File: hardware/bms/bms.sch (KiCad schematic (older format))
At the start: 199 parts, among them J1 Conn_01x08, J10 Conn_01x02, J11 Conn_01x02, J12 Conn_01x02, J13 Conn_01x10, J14 Conn_01x02, J15 Conn_01x02, J16 Cell Bypass, J2 Conn_01x04, J3 USB_B_Micro, J4 Conn_01x05, J5 Conn_01x04, J6 Conn_01x04, J7 Conn_01x03, J8 Conn_01x03, J9 Conn_01x02, M1 MountingHole, M2 MountingHole, M3 MountingHole, M4 MountingHole, M5 MountingHole, M6 MountingHole, Q1 BC817, Q10 ZXMP4A16G, Q11 IRF540N, Q12 IRF540N, Q13 BSS138, Q14 IRF540N, Q15 BSS138, Q16 BSS138, Q2 ZXMP4A16G, Q3 BSS138, Q4 BS170, Q5 IRF9540N, Q6 BC847, Q7 IRF9540N, Q8 BSS138, Q9 ZXMP4A16G, SW1 SW_DIP_x03, U1 USBLC6-2SC6, U2 STM32F042C6Tx, U3 TPS560430x3F, U4 TCAN334, U5 MAX485E, U6 LM5164DDAR, U7 LSI94202, Y1 8MHz

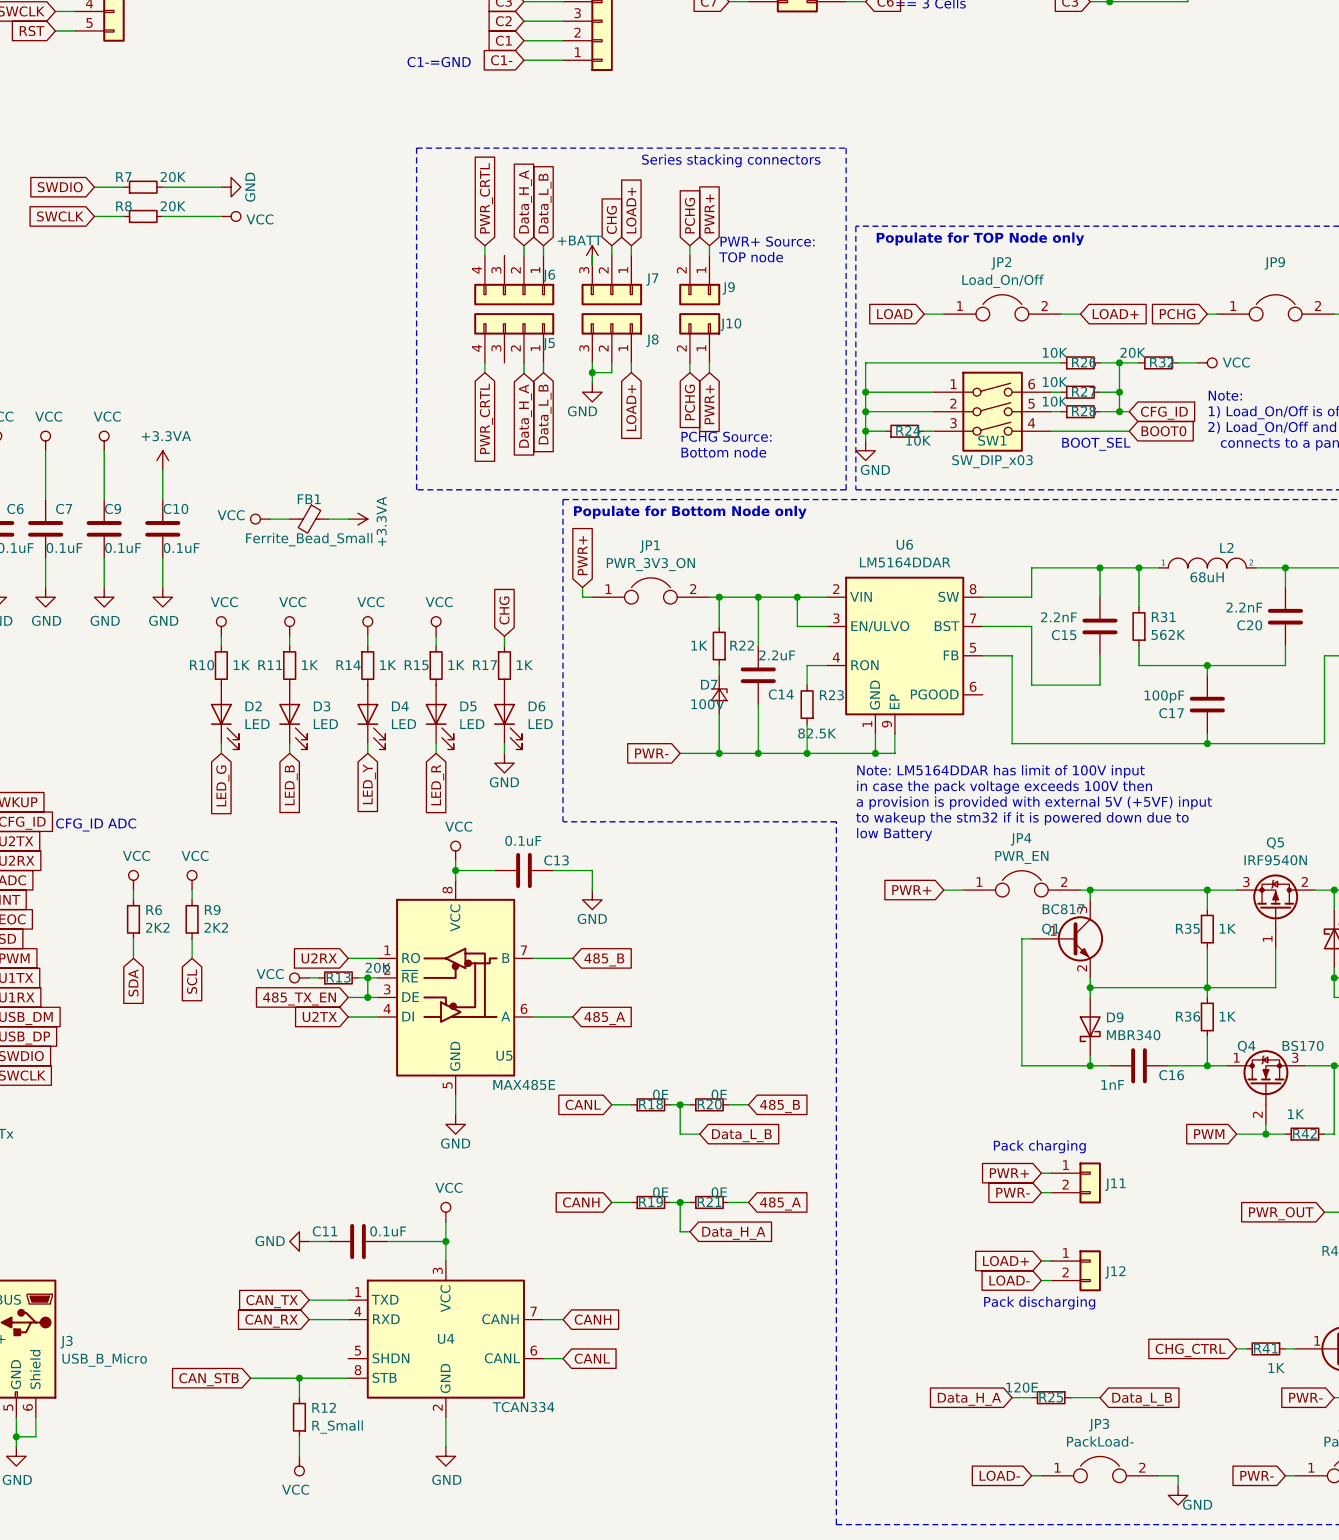
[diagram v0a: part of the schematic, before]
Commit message: Changed connection to support series and parallel stacking
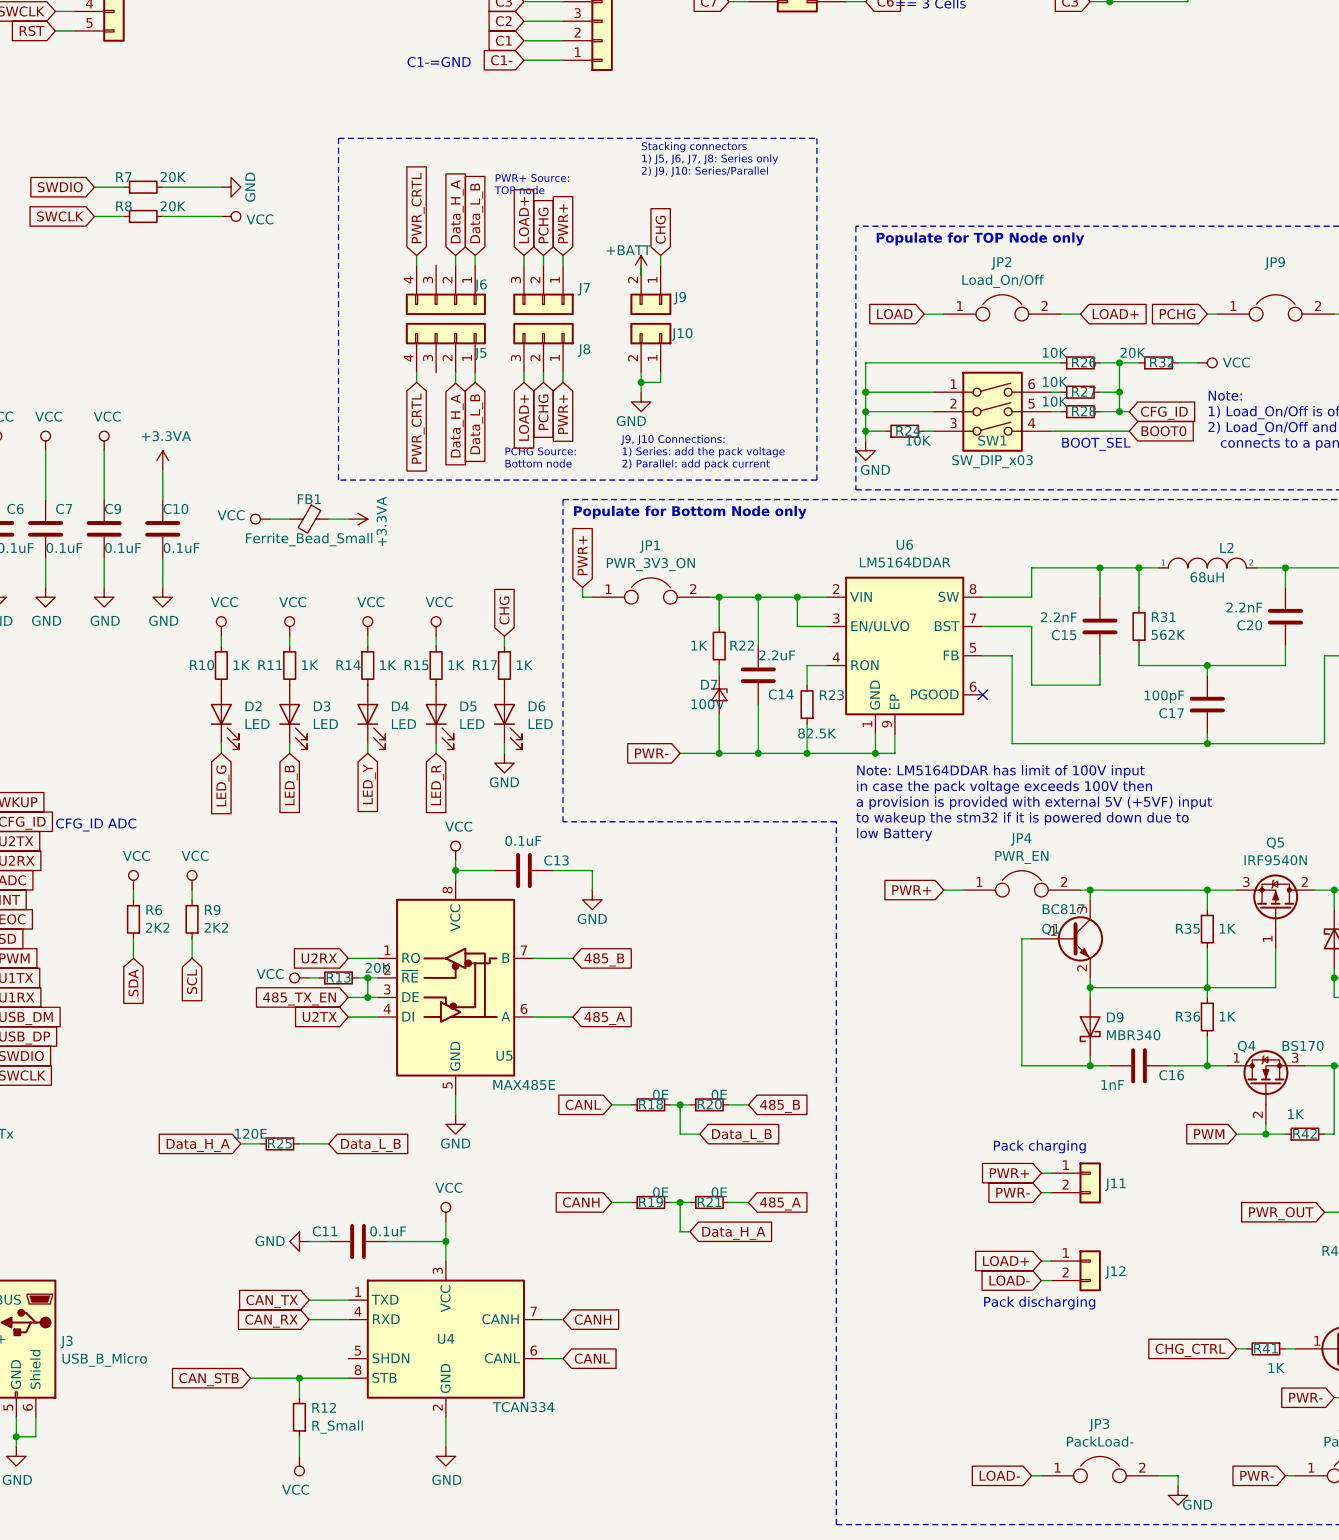
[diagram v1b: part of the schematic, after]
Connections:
- net +BATT: now also J9.2 (Pin_2); no longer J7.3 (Pin_3)
- net CHG: now also J9.1 (Pin_1); no longer J7.2 (Pin_2)
- net GND: now also J10.1 (Pin_1), J10.2 (Pin_2); no longer J8.2 (Pin_2), J8.3 (Pin_3)
- net LOAD+: now also J7.3 (Pin_3), J8.3 (Pin_3); no longer J7.1 (Pin_1), J8.1 (Pin_1)
- net PCHG: now also J7.2 (Pin_2), J8.2 (Pin_2); no longer J10.2 (Pin_2), J9.2 (Pin_2)
- net PWR+: now also J7.1 (Pin_1), J8.1 (Pin_1); no longer J10.1 (Pin_1), J9.1 (Pin_1)
- no-connect marks 6 -> 7
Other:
- note added: "J9, J10 Connections:\n1) Series: add the pack voltage\n2) Parallel: add pack current"
- note added: "Stacking connectors\n1) J5, J6, J7, J8: Series only\n2) J9, J10: Series/Parallel"
- note removed: "Series stacking connectors"
- moved on the sheet: J10, J5, J6, J7, J8, J9, R25
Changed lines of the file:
@@
 L Device:R_Small R25
 U 1 1 5E91A3BE
-P 8600 10400
-F 0 "R25" V 8600 10400 50  0000 C CNN
-F 1 "120E" V 8550 10250 50  0000 C CNN
-F 2 "Resistor_SMD:R_0603_1608Metric_Pad1.05x0.95mm_HandSolder" H 8600 10400 50  0001 C CNN
-F 3 "~" H 8600 10400 50  0001 C CNN
-	1    8600 10400
+P 4650 9100
+F 0 "R25" V 4650 9100 50  0000 C CNN
+F 1 "120E" V 4600 8950 50  0000 C CNN
+F 2 "Resistor_SMD:R_0603_1608Metric_Pad1.05x0.95mm_HandSolder" H 4650 9100 50  0001 C CNN
+F 3 "~" H 4650 9100 50  0001 C CNN
+	1    4650 9100
 	0    1    1    0
 $EndComp
-Text GLabel 8400 10400 0    50   Input ~ 0
+Text GLabel 4450 9100 0    50   Input ~ 0
 Data_H_A
-Text GLabel 8850 10400 2    50   Input ~ 0
+Text GLabel 4900 9100 2    50   Input ~ 0
 Data_L_B
 Wire Wire Line
-	8400 10400 8500 10400
+	4450 9100 4550 9100
 Wire Wire Line
-	8700 10400 8850 10400
+	4750 9100 4900 9100
 Text GLabel 5000 8450 0    50   Input ~ 0
 U2TX
@@
 L power:+BATT #PWR0144
 U 1 1 5F326BD9
-P 6250 4600
-F 0 "#PWR0144" H 6250 4450 50  0001 C CNN
-F 1 "+BATT" H 6184 4725 50  0000 C CNN
-F 2 "" H 6250 4600 50  0001 C CNN
-F 3 "" H 6250 4600 50  0001 C CNN
-	1    6250 4600
+P 6500 4650
+F 0 "#PWR0144" H 6500 4500 50  0001 C CNN
+F 1 "+BATT" H 6434 4775 50  0000 C CNN
+F 2 "" H 6500 4650 50  0001 C CNN
+F 3 "" H 6500 4650 50  0001 C CNN
+	1    6500 4650
 	1    0    0    -1
 $EndComp
 Wire Wire Line
-	6350 5100 6350 5150
-Text GLabel 5900 5154 3    50   Input ~ 0
+	6600 5150 6600 5200
+Text GLabel 5550 5204 3    50   Input ~ 0
 Data_H_A
-Text GLabel 6000 5150 3    50   Input ~ 0
+Text GLabel 5650 5200 3    50   Input ~ 0
 Data_L_B
 Connection ~ 12000 7500
@@
 Wire Wire Line
 	1400 8450 1750 8450
-Text GLabel 5700 5150 3    50   Input ~ 0
+Text GLabel 5350 5200 3    50   Input ~ 0
 PWR_CRTL
 Text GLabel 6750 9550 2    50   Input ~ 0
@@
 	9550 10150 9600 10150
 Wire Wire Line
-	6250 4600 6250 4550
+	6500 4650 6500 4600
 Wire Wire Line
-	6350 4500 6350 4550
+	6600 4550 6600 4600
 Wire Wire Line
-	6250 5200 6250 5150
-Text GLabel 6000 4500 1    50   Input ~ 0
+	6500 5250 6500 5200
+Text GLabel 5650 4550 1    50   Input ~ 0
 Data_L_B
-Text GLabel 5900 4500 1    50   Input ~ 0
+Text GLabel 5550 4550 1    50   Input ~ 0
 Data_H_A
-Text GLabel 6350 4500 1    50   Input ~ 0
+Text GLabel 6600 4550 1    50   Input ~ 0
 CHG
 $Comp
 L power:GND #PWR0147
 U 1 1 5E739987
-P 6250 5200
-F 0 "#PWR0147" H 6250 4950 50  0001 C CNN
-F 1 "GND" H 6200 5050 50  0000 C CNN
-F 2 "" H 6250 5200 50  0001 C CNN
-F 3 "" H 6250 5200 50  0001 C CNN
-	1    6250 5200
+P 6500 5250
+F 0 "#PWR0147" H 6500 5000 50  0001 C CNN
+F 1 "GND" H 6450 5100 50  0000 C CNN
+F 2 "" H 6500 5250 50  0001 C CNN
+F 3 "" H 6500 5250 50  0001 C CNN
+	1    6500 5250
 	1    0    0    -1
 $EndComp
@@
 L Connector_Generic:Conn_01x04 J5
 U 1 1 5E7A8731
-P 5900 4750
-F 0 "J5" V 6150 4850 50  0000 L CNN
-F 1 "Conn_01x04" H 5980 4651 50  0001 L CNN
-F 2 "Connector_Molex:Molex_KK-254_AE-6410-04A_1x04_P2.54mm_Vertical" H 5900 4750 50  0001 C CNN
-F 3 "~" H 5900 4750 50  0001 C CNN
-	1    5900 4750
+P 5550 4800
+F 0 "J5" V 5800 4900 50  0000 L CNN
+F 1 "Conn_01x04" H 5630 4701 50  0001 L CNN
+F 2 "Connector_Molex:Molex_KK-254_AE-6410-04A_1x04_P2.54mm_Vertical" H 5550 4800 50  0001 C CNN
+F 3 "~" H 5550 4800 50  0001 C CNN
+	1    5550 4800
 	0    1    1    0
 $EndComp
@@
 L Connector_Generic:Conn_01x04 J6
 U 1 1 5E96F1D5
-P 5900 4900
-F 0 "J6" V 6150 5000 50  0000 L CNN
-F 1 "Conn_01x04" H 5980 4801 50  0001 L CNN
-F 2 "Connector_Molex:Molex_KK-254_AE-6410-04A_1x04_P2.54mm_Vertical" H 5900 4900 50  0001 C CNN
-F 3 "~" H 5900 4900 50  0001 C CNN
-	1    5900 4900
+P 5550 4950
+F 0 "J6" V 5800 5050 50  0000 L CNN
+F 1 "Conn_01x04" H 5630 4851 50  0001 L CNN
+F 2 "Connector_Molex:Molex_KK-254_AE-6410-04A_1x04_P2.54mm_Vertical" H 5550 4950 50  0001 C CNN
+F 3 "~" H 5550 4950 50  0001 C CNN
+	1    5550 4950
 	0    1    -1   0
 $EndComp
 Wire Wire Line
-	5900 4500 5900 4550
+	5550 4550 5550 4600
 Wire Wire Line
-	6000 4500 6000 4550
+	5650 4550 5650 4600
 Wire Wire Line
-	5900 5100 5900 5154
+	5550 5150 5550 5204
 $Comp
 L Interface_UART:MAX485E U5
@@
 Text GLabel 10150 8700 2    50   Input ~ 0
 PWR-
-Text GLabel 6850 4500 1    50   Input ~ 0
+Text GLabel 6100 4550 1    50   Input ~ 0
 PWR+
-Text GLabel 6450 4500 1    50   Input ~ 0
+Text GLabel 5900 4550 1    50   Input ~ 0
 LOAD+
 Wire Wire Line
-	6450 4500 6450 4550
+	5900 4550 5900 4600
 Wire Wire Line
-	6450 5100 6450 5150
-Text GLabel 6450 5150 3    50   Input ~ 0
+	5900 5150 5900 5200
+Text GLabel 5900 5200 3    50   Input ~ 0
 LOAD+
-Text GLabel 6850 5150 3    50   Input ~ 0
+Text GLabel 6100 5200 3    50   Input ~ 0
 PWR+
 $Comp
@@
 L BMS:Conn_01x02 J9
 U 1 1 6179076C
-P 6850 4750
-F 0 "J9" V 6814 4821 50  0000 L CNN
-F 1 "Conn_01x02" H 6930 4651 50  0001 L CNN
-F 2 "TerminalBlock:TerminalBlock_bornier-2_P5.08mm" H 6850 4750 50  0001 C CNN
-F 3 "" H 6850 4750 50  0001 C CNN
-	1    6850 4750
+P 6600 4800
+F 0 "J9" V 6564 4871 50  0000 L CNN
+F 1 "Conn_01x02" H 6680 4701 50  0001 L CNN
+F 2 "TerminalBlock:TerminalBlock_bornier-2_P5.08mm" H 6600 4800 50  0001 C CNN
+F 3 "" H 6600 4800 50  0001 C CNN
+	1    6600 4800
 	0    1    1    0
 $EndComp
@@
 L BMS:Conn_01x02 J10
 U 1 1 61790D23
-P 6850 4900
-F 0 "J10" V 6850 4960 50  0000 L CNN
-F 1 "Conn_01x02" H 6930 4801 50  0001 L CNN
-F 2 "TerminalBlock:TerminalBlock_bornier-2_P5.08mm" H 6850 4900 50  0001 C CNN
-F 3 "" H 6850 4900 50  0001 C CNN
-	1    6850 4900
+P 6600 4950
+F 0 "J10" V 6600 5010 50  0000 L CNN
+F 1 "Conn_01x02" H 6680 4851 50  0001 L CNN
+F 2 "TerminalBlock:TerminalBlock_bornier-2_P5.08mm" H 6600 4950 50  0001 C CNN
+F 3 "" H 6600 4950 50  0001 C CNN
+	1    6600 4950
 	0    1    -1   0
 $EndComp
 Wire Wire Line
-	6850 4550 6850 4500
+	6100 4600 6100 4550
 Wire Wire Line
-	6850 5100 6850 5150
+	6100 5150 6100 5200
 Wire Wire Line
 	12000 7450 12000 7500
@@
 Wire Wire Line
 	14200 9600 14200 9650
-Text Notes 6900 4600 0    50   ~ 0
+Text Notes 5750 4250 0    39   ~ 0
 PWR+ Source:\nTOP node
-Text Notes 6700 5600 0    50   ~ 0
+Text Notes 5800 5650 0    39   ~ 0
 PCHG Source:\nBottom node
 Wire Wire Line
@@
 Wire Wire Line
 	10900 8400 10950 8400
-Text GLabel 6750 4500 1    50   Input ~ 0
+Text GLabel 6000 4550 1    50   Input ~ 0
 PCHG
-Text GLabel 6750 5150 3    50   Input ~ 0
+Text GLabel 6000 5200 3    50   Input ~ 0
 PCHG
 Wire Wire Line
-	6750 4500 6750 4550
+	6000 4550 6000 4600
 Wire Wire Line
-	6750 5100 6750 5150
+	6000 5150 6000 5200
 Text Notes 8300 9150 0    50   ~ 0
 Pack charging
 Text Notes 8250 9950 0    50   ~ 0
 Pack discharging
-$Comp
-L Connector_Generic:Conn_01x03 J7
-U 1 1 5F75BC62
-P 6350 4750
-F 0 "J7" V 6268 4930 50  0000 L CNN
-F 1 "Conn_01x03" V 6313 4930 50  0001 L CNN
-F 2 "TerminalBlock:TerminalBlock_bornier-3_P5.08mm" H 6350 4750 50  0001 C CNN
-F 3 "~" H 6350 4750 50  0001 C CNN
-	1    6350 4750
-	0    1    1    0
-$EndComp
-$Comp
-L Connector_Generic:Conn_01x03 J8
-U 1 1 5F7CDFE8
-P 6350 4900
-F 0 "J8" V 6268 5080 50  0000 L CNN
-F 1 "Conn_01x03" V 6223 5080 50  0001 L CNN
-F 2 "TerminalBlock:TerminalBlock_bornier-3_P5.08mm" H 6350 4900 50  0001 C CNN
-F 3 "~" H 6350 4900 50  0001 C CNN
-	1    6350 4900
-	0    1    -1   0
-$EndComp
 Wire Wire Line
-	6350 5150 6250 5150
-Connection ~ 6250 5150
+	6600 5200 6500 5200
+Connection ~ 6500 5200
 Wire Wire Line
-	6250 5150 6250 5100
-Text Notes 6500 4100 0    50   ~ 0
-Series stacking connectors
+	6500 5200 6500 5150
+Text Notes 6500 4150 0    39   ~ 0
+Stacking connectors\n1) J5, J6, J7, J8: Series only\n2) J9, J10: Series/Parallel
 Wire Wire Line
-	5700 4500 5700 4550
-Text GLabel 5700 4500 1    50   Input ~ 0
+	5350 4550 5350 4600
+Text GLabel 5350 4550 1    50   Input ~ 0
 PWR_CRTL
 Wire Notes Line
-	5350 4000 7550 4000
+	4950 3950 7400 3950
 Wire Notes Line
-	7550 4000 7550 5750
+	7400 3950 7400 5700
 Wire Notes Line
-	7550 5750 5350 5750
+	7400 5700 4950 5700
 Wire Notes Line
-	5350 5750 5350 4000
+	4950 5700 4950 3950
 Wire Wire Line
-	5700 5100 5700 5150
+	5350 5150 5350 5200
 Wire Wire Line
-	6000 5100 6000 5150
+	5650 5150 5650 5200
 Wire Wire Line
 	1100 4800 1100 4750
@@
 	8750 7800 8800 7800
 Connection ~ 8800 7800
+NoConn ~ 8250 6800
+Text Notes 6400 5650 0    39   ~ 0
+J9, J10 Connections:\n1) Series: add the pack voltage\n2) Parallel: add pack current
+$Comp
+L Connector_Generic:Conn_01x03 J8
+U 1 1 5F7CDFE8
+P 6000 4950
+F 0 "J8" V 5918 5130 50  0000 L CNN
+F 1 "Conn_01x03" V 5873 5130 50  0001 L CNN
+F 2 "TerminalBlock:TerminalBlock_bornier-3_P5.08mm" H 6000 4950 50  0001 C CNN
+F 3 "~" H 6000 4950 50  0001 C CNN
+	1    6000 4950
+	0    1    -1   0
+$EndComp
+$Comp
+L Connector_Generic:Conn_01x03 J7
+U 1 1 5F75BC62
+P 6000 4800
+F 0 "J7" V 5918 4980 50  0000 L CNN
+F 1 "Conn_01x03" V 5963 4980 50  0001 L CNN
+F 2 "TerminalBlock:TerminalBlock_bornier-3_P5.08mm" H 6000 4800 50  0001 C CNN
+F 3 "~" H 6000 4800 50  0001 C CNN
+	1    6000 4800
+	0    1    1    0
+$EndComp
 $EndSCHEMATC

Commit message: created netlist
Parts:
- U1: footprint TO_SOT_Packages_SMD:SOT-23-6 -> Package_SO:TSOP-6_1.65x3.05mm_P0.95mm
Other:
- moved on the sheet: C14, C15, C17, C18, C19, C20, C21, C24, C26, C27, C28, C29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
